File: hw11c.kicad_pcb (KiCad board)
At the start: 2 copper layers, 49 x 27.5 mm, 83 parts, among them Q1 KX-7_12MHZ, SW1 BUTT1, SW2 BUTT2, X1 ~RESET, X10 PIO2.8, X11 PIO1.4, X12 ADC3, X13 PIO0.8, X14 PIO0.9, X15 MAT0, X16 PIO0.6, X17 PIO0.7, X2 SWCLK, X3 SWDIO, X4 SSEL1, X5 SCK1, X6 MISO1, X7 MOSI1, X8 PIO2.6, X9 PIO2.7

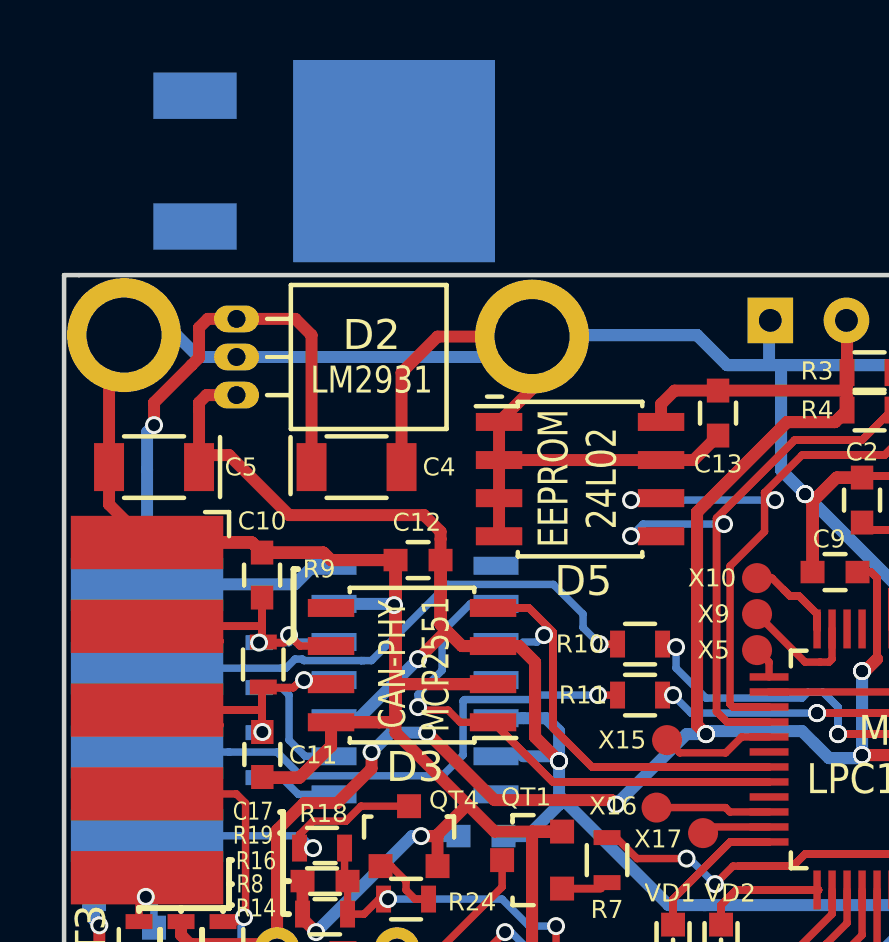
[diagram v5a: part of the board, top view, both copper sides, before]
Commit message: Add LM78M05 to board. It used as alternate DC-DC for applications with current consumption more 100mA.
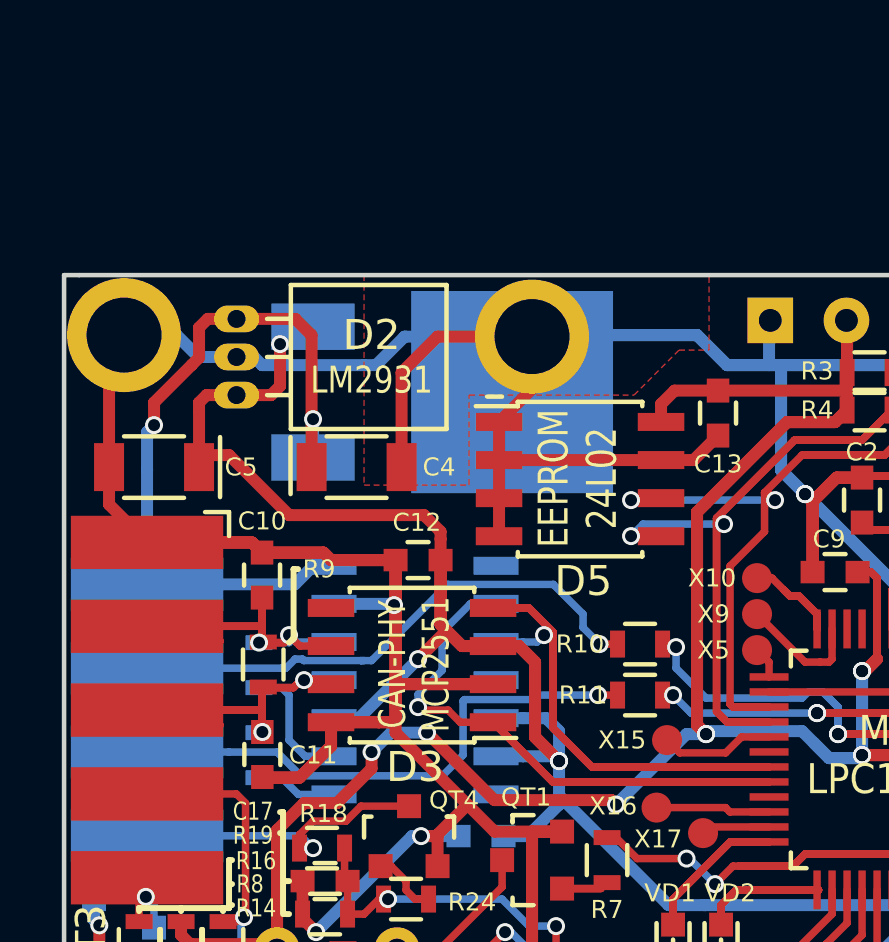
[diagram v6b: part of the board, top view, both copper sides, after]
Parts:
- moved D7 8.65 mm to (62.5, 53.9)
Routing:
- net /5V: track 98.3 -> 103.5 mm, vias 8 -> 9
- net GND: track 498.3 -> 501.3 mm
- net /12V: track 24.3 -> 25.6 mm, vias 1 -> 2
- net /CAN_RX: track 27.6 -> 28.5 mm
- added copper zone on F.Cu, net GND
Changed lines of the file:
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@@
   (general
     (links 178)
-    (no_connects 7)
-    (area 49.824999 49.924999 98.975001 77.575001)
+    (no_connects 0)
+    (area 49.345 42.329999 117.971429 90.700001)
     (thickness 1.6)
     (drawings 51)
-    (tracks 1089)
+    (tracks 1108)
     (zones 0)
     (modules 83)
@@
   )
   (module libs:D-Pak_TO252AA (layer B.Cu)
-    (at 58.565 46.2 90)
+    (at 62.5 53.9 90)
     (descr "D-Pak, TO252AA, Diode")
     (tags "D-Pak TO252AA Diode")
     (attr smd)
-    (fp_text reference D7 (at 0 7.5 90) (layer B.SilkS)
+    (fp_text reference D7 (at 1.7 6.8 180) (layer B.SilkS)
       (effects (font (size 1 1) (thickness 0.15)) (justify mirror))
     )
-    (fp_text value 78M05 (at 0 -8.1 90) (layer B.Fab)
+    (fp_text value 78M05 (at 0.5 1.6 180) (layer B.Fab) hide
       (effects (font (size 1 1) (thickness 0.15)) (justify mirror))
     )
@@
     (effects (font (size 1 0.8) (thickness 0.15)))
   )
-  (gr_text "igorkov / BCOMP11\nigorkov.org/bcomp11v2\n2018 / version 2.3" (at 79.3 57.725) (layer B.SilkS)
+  (gr_text "igorkov / BCOMP11\nigorkov.org/bcomp11v2\n2018 / version 2.3" (at 79.8 61.4) (layer B.SilkS)
     (effects (font (size 1.5 1.5) (thickness 0.25)) (justify mirror))
   )
@@
   (segment (start 78 60.63641) (end 78 60.9) (width 0.25) (layer F.Cu) (net 1))
   (segment (start 78 60.9) (end 78 61.8) (width 0.25) (layer F.Cu) (net 1))
+  (segment (start 55.65 52.73) (end 56.23 52.73) (width 0.4) (layer B.Cu) (net 2))
+  (segment (start 56.23 52.73) (end 56.5 53) (width 0.4) (layer B.Cu) (net 2))
+  (segment (start 61.25 52.05) (end 65.5 52.05) (width 0.4) (layer B.Cu) (net 2))
+  (segment (start 60.3 53) (end 61.25 52.05) (width 0.4) (layer B.Cu) (net 2))
+  (segment (start 59.9 53) (end 60.3 53) (width 0.4) (layer B.Cu) (net 2))
+  (segment (start 56.5 53) (end 59.9 53) (width 0.4) (layer B.Cu) (net 2))
+  (segment (start 55.65 52.73) (end 54.38 52.73) (width 0.4) (layer B.Cu) (net 2))
+  (segment (start 54.38 52.73) (end 53.65 52) (width 0.4) (layer B.Cu) (net 2))
+  (segment (start 53.65 52) (end 51.9 52) (width 0.4) (layer B.Cu) (net 2))
   (segment (start 63.05 68.7) (end 61.8 68.7) (width 0.4) (layer B.Cu) (net 2))
   (segment (start 58.75076 75.475) (end 58.425 75.475) (width 0.4) (layer B.Cu) (net 2))
@@
   (segment (start 63.35 67.65) (end 64.25 68.55) (width 0.4) (layer F.Cu) (net 2))
   (segment (start 51.9 52) (end 53.65 52) (width 0.4) (layer B.Cu) (net 2))
-  (segment (start 53.65 52) (end 54.38 52.73) (width 0.4) (layer B.Cu) (net 2))
-  (segment (start 54.38 52.73) (end 64.82 52.73) (width 0.4) (layer B.Cu) (net 2))
   (segment (start 64.82 52.73) (end 65.5 52.05) (width 0.4) (layer B.Cu) (net 2))
   (segment (start 61.15 56) (end 61.15 53.25) (width 0.4) (layer F.Cu) (net 2))
@@
   (segment (start 77.5 60.5) (end 78.35 59.65) (width 0.25) (layer F.Cu) (net 3))
   (segment (start 77.5 61.8) (end 77.5 60.5) (width 0.25) (layer F.Cu) (net 3))
+  (segment (start 58.2 56.08) (end 58.2 54.8) (width 0.4) (layer B.Cu) (net 4))
+  (segment (start 58.2 54.8) (end 58.15 54.8) (width 0.4) (layer F.Cu) (net 4))
+  (via (at 58.2 54.8) (size 0.6) (drill 0.4) (layers F.Cu B.Cu) (net 4))
   (segment (start 58.21 59.69) (end 57.591 60.309) (width 0.4) (layer B.Cu) (net 4))
   (segment (start 55.65 51.46) (end 57.61 51.46) (width 0.4) (layer F.Cu) (net 4))
-  (segment (start 58.15 52) (end 58.15 56) (width 0.4) (layer F.Cu) (net 4))
+  (segment (start 58.15 52) (end 58.15 54.8) (width 0.4) (layer F.Cu) (net 4))
+  (segment (start 58.15 54.8) (end 58.15 56) (width 0.4) (layer F.Cu) (net 4))
   (segment (start 57.61 51.46) (end 58.15 52) (width 0.4) (layer F.Cu) (net 4))
   (segment (start 54.4 52.75) (end 54.4 51.75) (width 0.4) (layer F.Cu) (net 4))
@@
   (segment (start 52.667 56.5) (end 52.667 56.483) (width 0.4) (layer B.Cu) (net 4))
   (segment (start 52.209 60.309) (end 52.667 60.309) (width 0.4) (layer B.Cu) (net 4))
+  (segment (start 55.65 54) (end 56.8 54) (width 0.4) (layer F.Cu) (net 5))
+  (segment (start 57.1 52.3) (end 57.68 51.72) (width 0.4) (layer B.Cu) (net 5))
+  (via (at 57.1 52.3) (size 0.6) (drill 0.4) (layers F.Cu B.Cu) (net 5))
+  (segment (start 57.1 53.7) (end 57.1 52.3) (width 0.4) (layer F.Cu) (net 5))
+  (segment (start 56.8 54) (end 57.1 53.7) (width 0.4) (layer F.Cu) (net 5))
+  (segment (start 57.68 51.72) (end 58.2 51.72) (width 0.4) (layer B.Cu) (net 5))
+  (segment (start 64.3 66.04) (end 65.202 66.04) (width 0.4) (layer B.Cu) (net 5))
+  (segment (start 66.24 66.04) (end 66.4 66.2) (width 0.4) (layer B.Cu) (net 5))
+  (segment (start 65.202 66.04) (end 66.24 66.04) (width 0.4) (layer B.Cu) (net 5))
   (segment (start 64.55 68.7) (end 65.35 68.7) (width 0.4) (layer B.Cu) (net 5))
   (segment (start 65.35 68.7) (end 66.4 67.65) (width 0.4) (layer B.Cu) (net 5))
@@
   (segment (start 66.4 67.35) (end 66.4 66.2) (width 0.4) (layer B.Cu) (net 5))
   (segment (start 70.05 71) (end 66.4 67.35) (width 0.4) (layer B.Cu) (net 5))
-  (segment (start 65.202 66.04) (end 66.24 66.04) (width 0.4) (layer B.Cu) (net 5))
-  (segment (start 66.24 66.04) (end 66.4 66.2) (width 0.4) (layer B.Cu) (net 5))
   (segment (start 65.202 64.77) (end 65.97 64.77) (width 0.4) (layer B.Cu) (net 5))
   (segment (start 65.97 64.77) (end 66.4 65.2) (width 0.4) (layer B.Cu) (net 5))
@@
   (segment (start 71.954998 65.925) (end 70.425 65.925) (width 0.25) (layer F.Cu) (net 19))
   (segment (start 72.485098 65.3949) (end 71.954998 65.925) (width 0.25) (layer F.Cu) (net 19))
-  (segment (start 66.2 62) (end 65.9 62) (width 0.25) (layer F.Cu) (net 21))
-  (segment (start 65.9 62) (end 65.67 62.23) (width 0.25) (layer B.Cu) (net 21))
-  (via (at 65.9 62) (size 0.6) (drill 0.4) (layers F.Cu B.Cu) (net 21))
+  (segment (start 64.3 62.23) (end 65.202 62.23) (width 0.25) (layer B.Cu) (net 21))
   (segment (start 65.67 62.23) (end 65.202 62.23) (width 0.25) (layer B.Cu) (net 21))
+  (via (at 65.9 62) (size 0.6) (drill 0.4) (layers F.Cu B.Cu) (net 21))
+  (segment (start 65.9 62) (end 65.67 62.23) (width 0.25) (layer B.Cu) (net 21))
+  (segment (start 65.9 62) (end 66.2 62) (width 0.25) (layer F.Cu) (net 21))
   (segment (start 64.2 61.095) (end 64.205 61.1) (width 0.25) (layer F.Cu) (net 21))
   (segment (start 67.5 66.4) (end 66.2 65.1) (width 0.25) (layer F.Cu) (net 21))
@@
     (connect_pads yes (clearance 0.4))
     (min_thickness 0.4)
-    (fill (arc_segments 16) (thermal_gap 0.508) (thermal_bridge_width 0.508))
+    (fill yes (arc_segments 16) (thermal_gap 0.508) (thermal_bridge_width 0.508))
     (polygon
       (pts
@@
       )
     )
+  )
+  (zone (net 2) (net_name GND) (layer F.Cu) (hatch edge 0.508)
+    (connect_pads yes (clearance 0.4))
+    (min_thickness 0.4)
+    (fill yes (arc_segments 16) (thermal_gap 0.508) (thermal_bridge_width 0.508))
+    (polygon
+      (pts
+        (xy 59.9 50) (xy 59.9 57) (xy 63.4 57) (xy 63.4 54) (xy 68.9 54)
+        (xy 70.4 52.5) (xy 71.4 52.5) (xy 71.4 50)
+      )
+    )

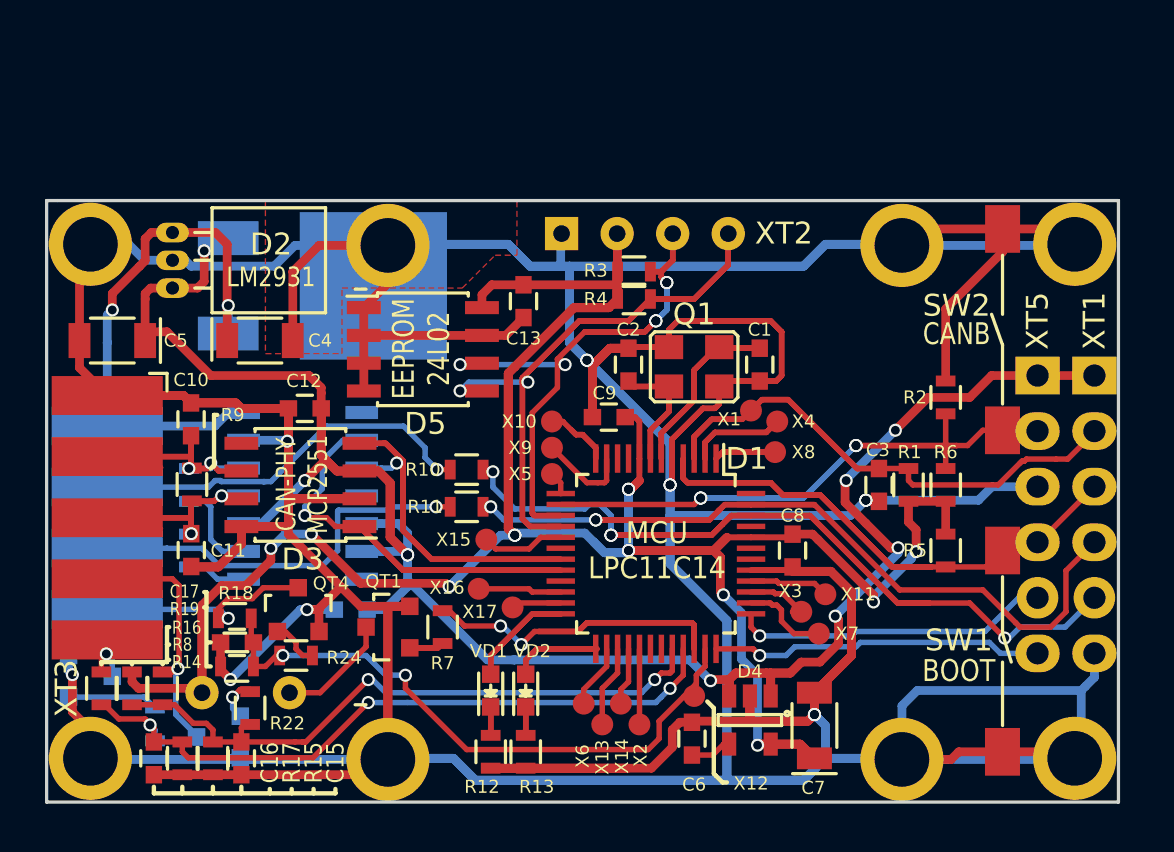
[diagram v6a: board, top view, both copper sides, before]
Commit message: Add resistive divider on ADC5 (AIN4) for system voltage measurement. Add reference voltage for AIN2. Add information on scheme.
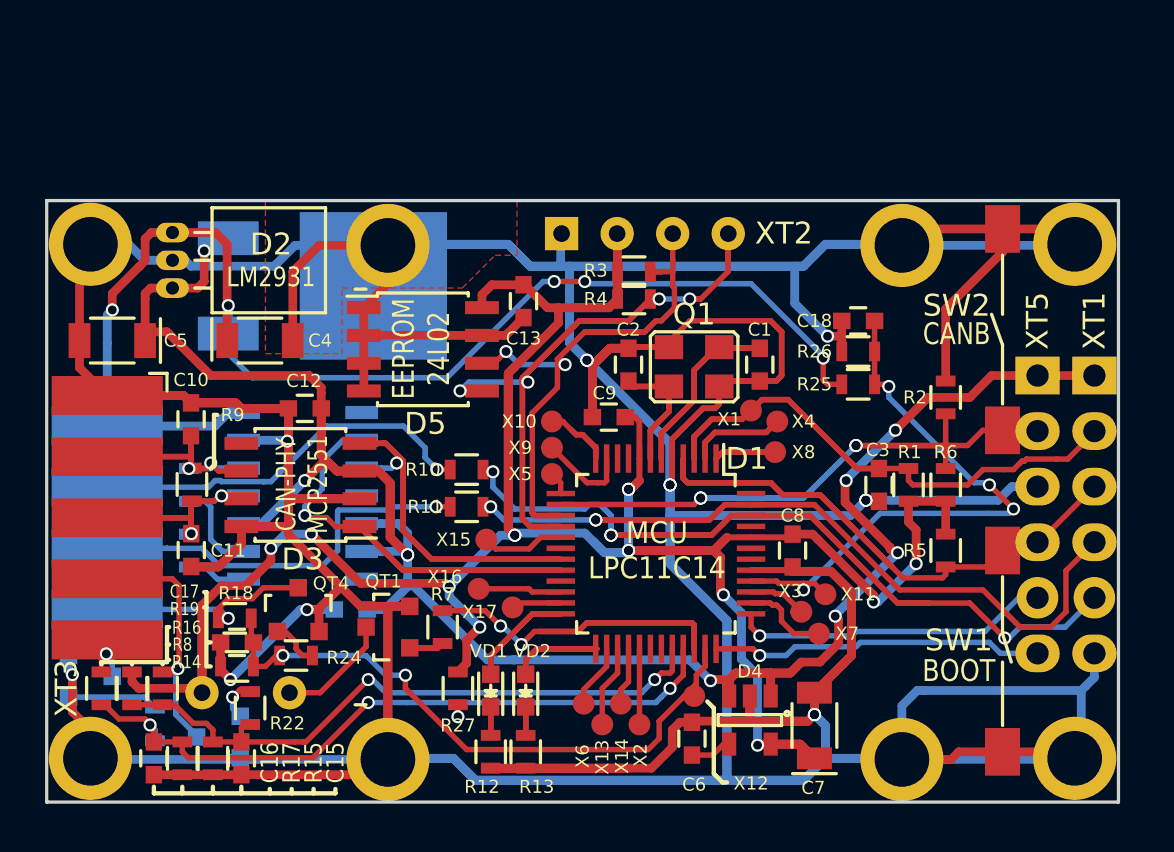
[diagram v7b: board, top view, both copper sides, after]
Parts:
- added C18: 0.1, libs:C_0603, F.Cu at (87.0, 55.5)
- added R25: 33k, libs:R_0603, F.Cu at (87.0, 58.4)
- added R26: 4.7k, libs:R_0603, F.Cu at (87.0, 56.9)
- added R27: 10k, libs:R_0603, F.Cu at (68.7, 72.3)
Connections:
- net Net-(D1-Pad40) renamed /ADC5
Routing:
- net /12V: track 25.6 -> 60.2 mm, vias 2 -> 5
- net /ADC5: track 3.93 -> 27.3 mm, vias 0 -> 4
- net /I2C_SCL: track 35.3 -> 29.7 mm, vias 6 -> 2
- net /I2C_SDA: track 47.3 -> 43.2 mm, vias 2 -> 4
- net /BOOT: track 36.9 -> 35.6 mm
- net /ADC1: track 31.9 -> 33.1 mm, vias 3 -> 4
- net /3.3V: track 137.7 -> 137.0 mm, vias 13 -> 14
- net GND: track 501.3 -> 501.2 mm, vias 12 -> 13

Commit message: Add X18 pad.
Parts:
- added X18: ADC6, libs:PAD, F.Cu at (77.0, 74.2)
- moved X6 1.59 mm to (73.3, 74.1)
- moved X14 1.53 mm to (75.2, 74.2)
- moved X13 1.19 mm to (74.3, 73.3)
- moved X2 1.11 mm to (76.1, 73.3)
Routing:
- net Net-(D1-Pad30): track 0.00 -> 3.71 mm
- net Net-(D1-Pad25): track 8.32 -> 5.42 mm
- net /SO: track 2.94 -> 4.87 mm
- net Net-(D1-Pad28): track 2.65 -> 4.40 mm
